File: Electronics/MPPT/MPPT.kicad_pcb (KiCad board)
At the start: 2 copper layers, 169.5 x 123.8 mm, 128 parts, among them J1 Solar Array, J2 Battery, J3 Car Power, J4 CAN_In, J5 CAN_Out, Q1 200N25N, Q2 200N25N, SW1 RESET, SW2 CAN Address, U1 PQMC3-D12-S9-S, U2 Nucleo_L432KC, U3 UCC37321, U4 INA210, U5 ADM3055E, U6 INA210, U7 CDSOT23-T24CAN

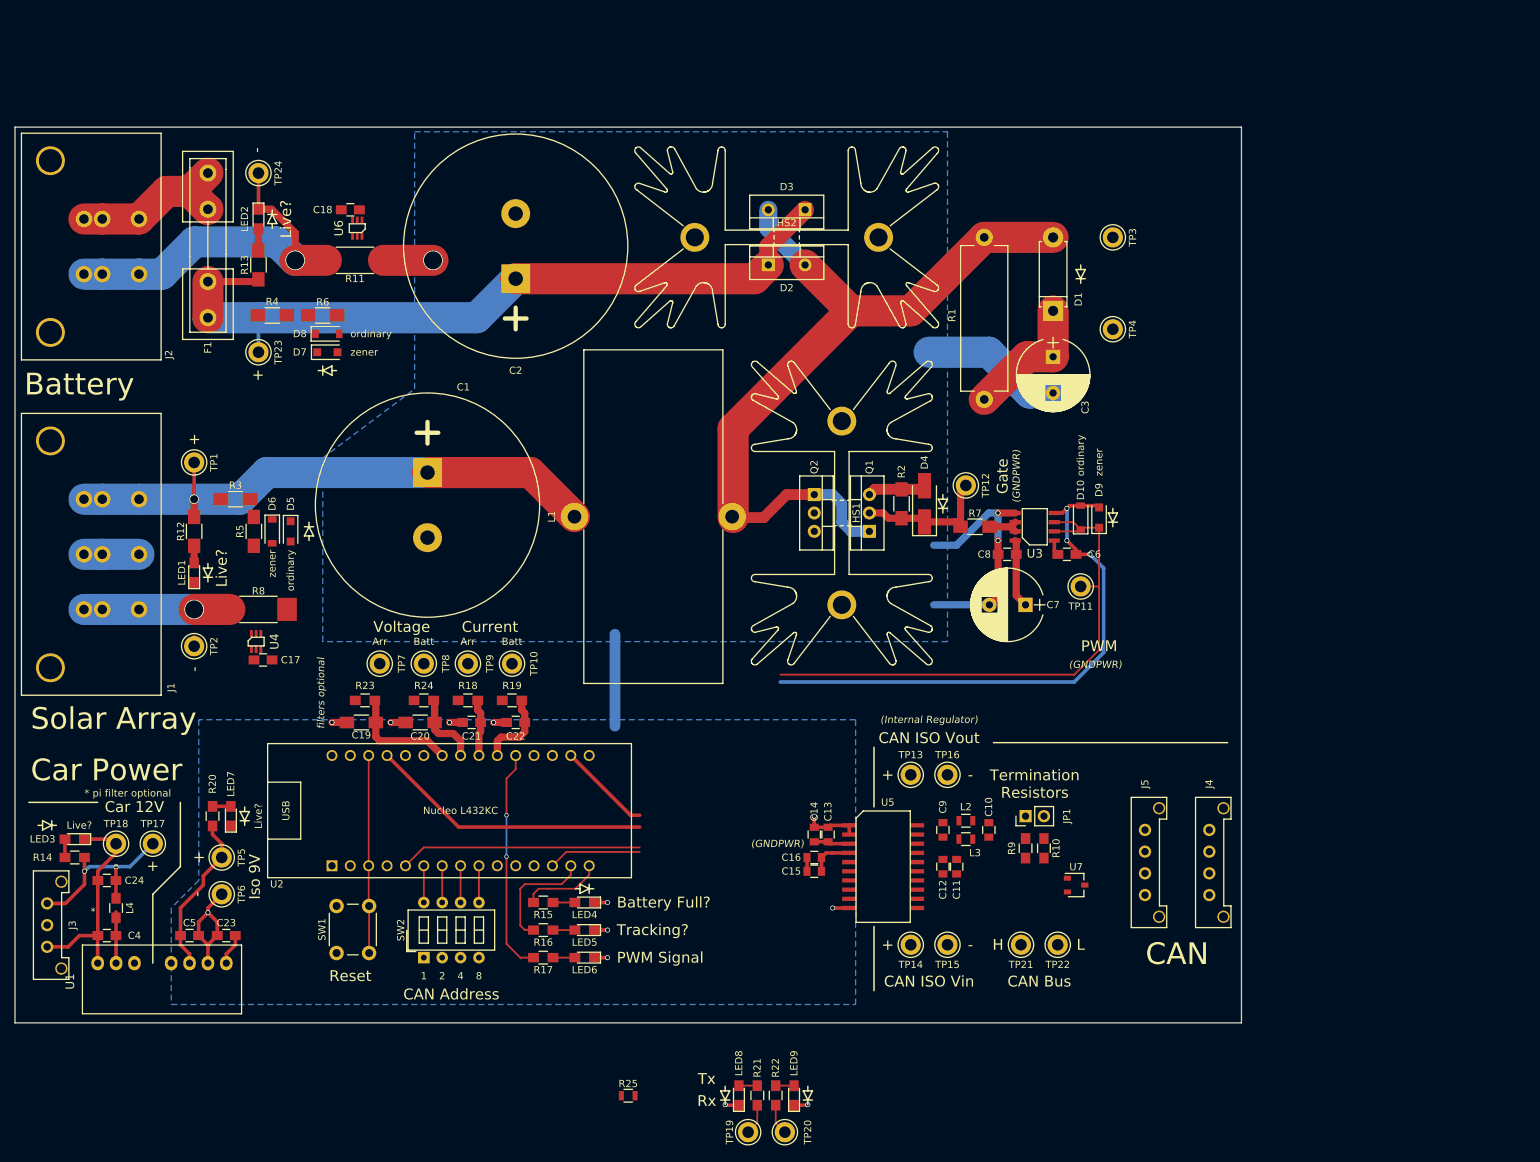
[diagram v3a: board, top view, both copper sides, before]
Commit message: MPPT: Moved CAN block to more compact location; shrunk board size.
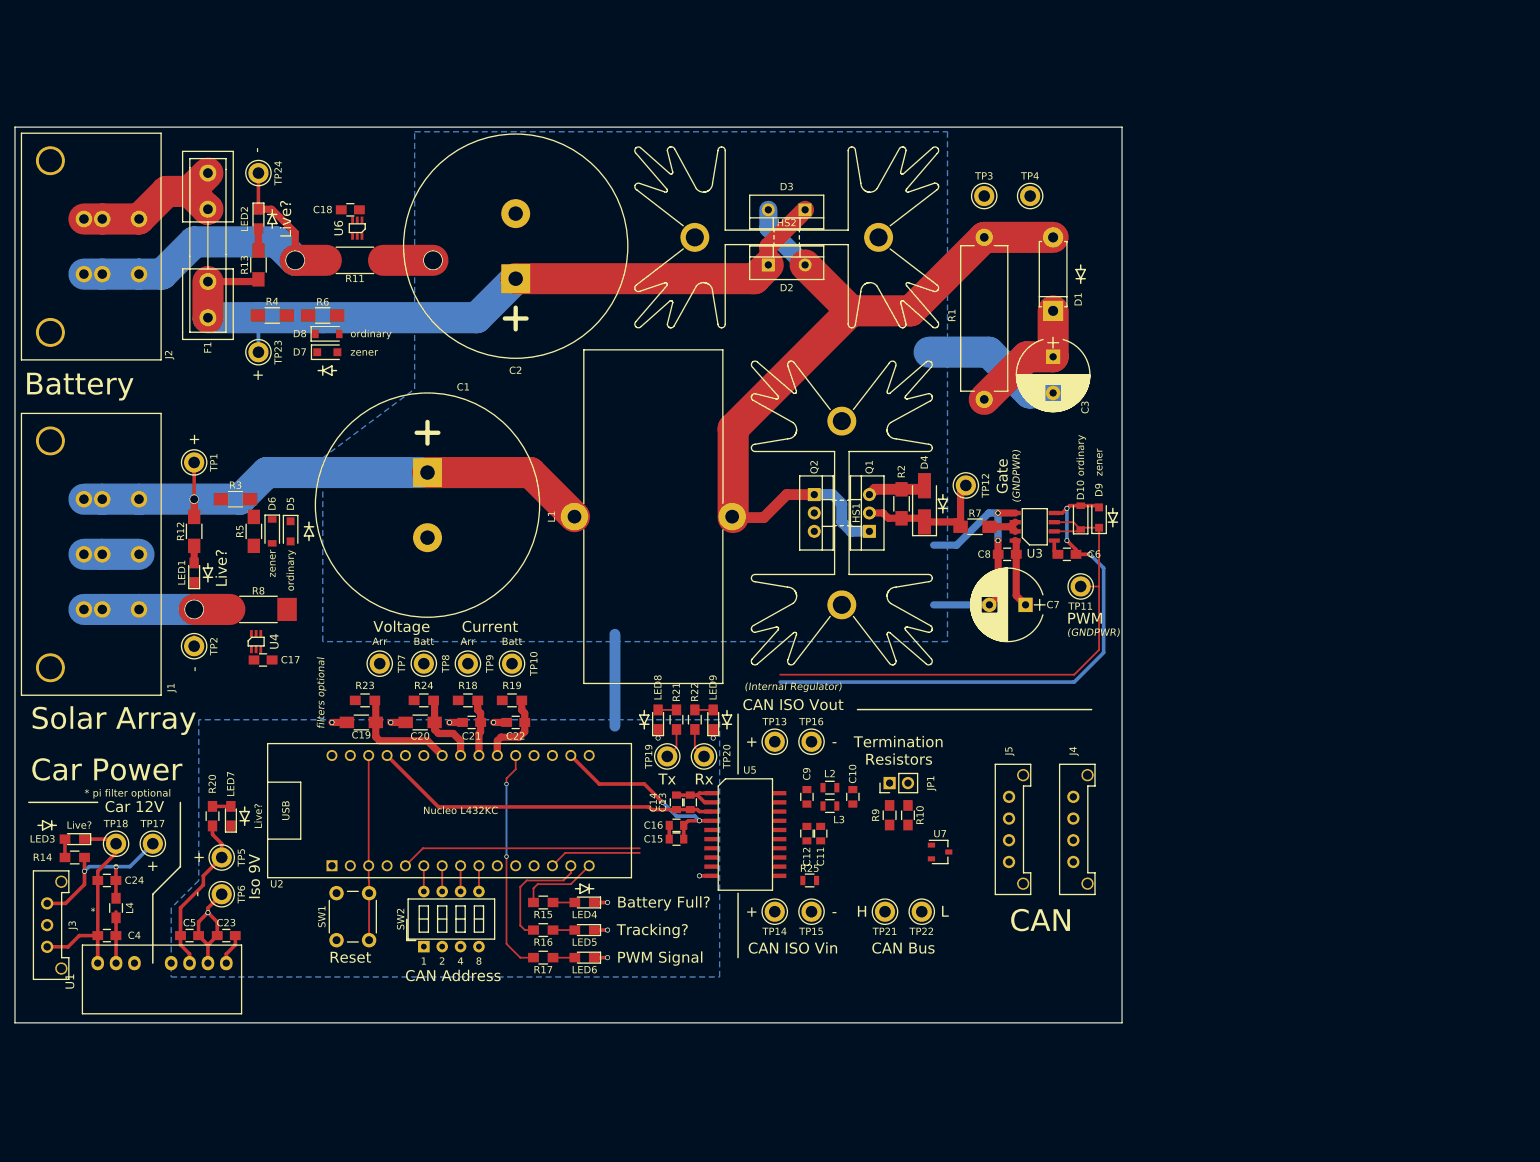
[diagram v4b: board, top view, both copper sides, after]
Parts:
- moved LED8 53.1 mm to (120.0, 113.0)
- moved LED9 53.1 mm to (127.6, 113.0)
- moved R21 53.1 mm to (122.6, 113.0)
- moved R22 53.1 mm to (125.1, 113.0)
- moved REF** 53.1 mm to (129.5, 113.0)
- moved REF** 53.1 mm to (118.1, 113.0)
- moved TP19 53.1 mm to (121.3, 118.1)
- moved TP20 53.1 mm to (126.4, 118.1)
- moved R25 38.9 mm to (141.0, 135.3)
- moved TP4 21.7 mm to (171.4, 40.6), turned to 0 degrees
- moved C13 19.6 mm to (124.5, 124.5)
- moved C15 19.6 mm to (122.6, 129.5)
- moved C14 19.6 mm to (122.6, 124.5)
- moved C16 19.6 mm to (122.6, 127.6)
- moved U5 19.6 mm to (132.1, 128.9)
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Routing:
- net +3V3: track 18.9 -> 27.5 mm, vias 0 -> 2
- net +5V: track 44.0 -> 48.0 mm
- net GNDPWR: track 189.9 -> 187.4 mm, vias 18 -> 17
- net /Reset: track 27.3 -> 25.5 mm
- net Net-(SW2-Pad8): track 5.08 -> 3.56 mm
- net Net-(SW2-Pad7): track 5.08 -> 3.56 mm
- net Net-(SW2-Pad6): track 5.08 -> 3.56 mm
- net Net-(SW2-Pad5): track 5.08 -> 3.56 mm
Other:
- board size 169.5 x 123.8 mm -> 153 x 123.8 mm

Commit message: MPPT: Move Car Power and Solar Array blocks to more compact locations; resize board.
Board is now 4.7x6.0in, and that's likely final.
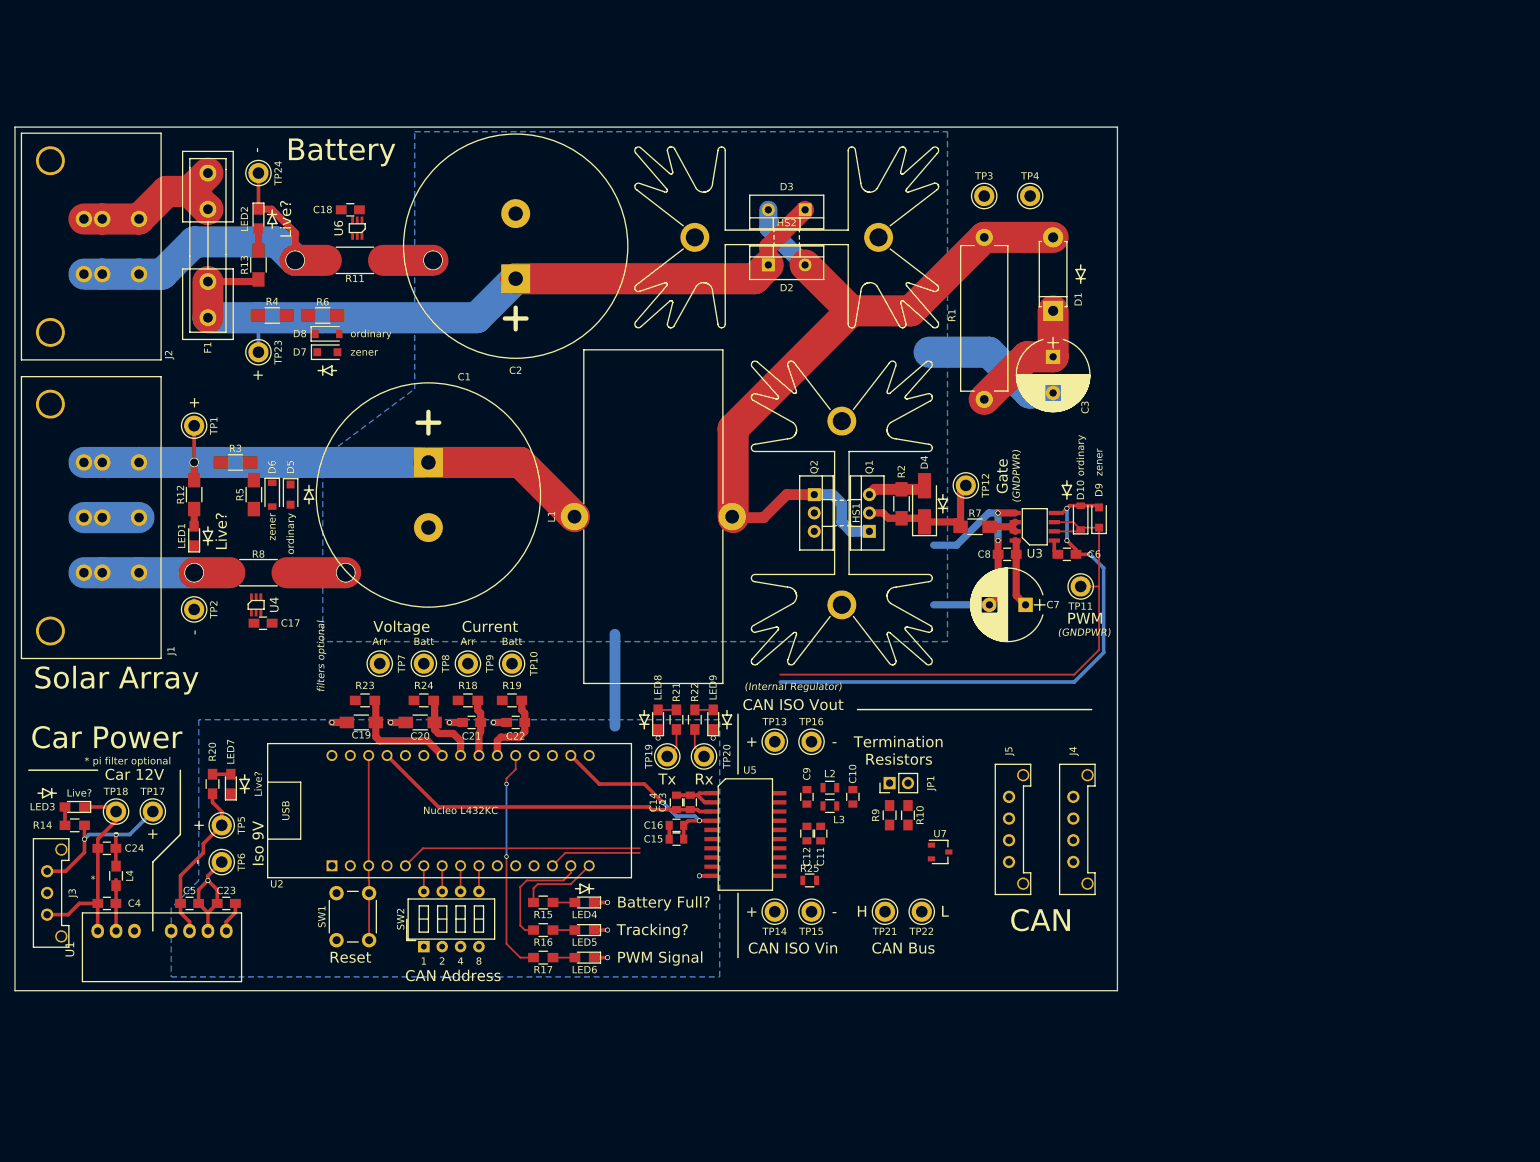
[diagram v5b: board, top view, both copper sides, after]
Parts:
- moved REF** 7.41 mm to (176.5, 81.3)
- moved C17 5.08 mm to (65.4, 99.7)
- moved R8 5.08 mm to (64.8, 92.7)
- moved D5 5.08 mm to (69.2, 81.9)
- moved D6 5.08 mm to (66.7, 81.9)
- moved J1 5.08 mm to (48.3, 77.5)
- moved LED1 5.08 mm to (55.9, 87.6)
- moved R12 5.08 mm to (55.9, 81.9)
- moved R3 5.08 mm to (61.6, 77.5)
- moved R5 5.08 mm to (64.1, 81.9)
- moved REF** 5.08 mm to (71.8, 81.9)
- moved REF** 5.08 mm to (57.8, 87.6)
- moved TP1 5.08 mm to (55.9, 72.4)
- moved TP2 5.08 mm to (55.9, 97.8)
- moved U4 5.08 mm to (64.4, 97.2)
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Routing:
- net GNDPWR: track 187.4 -> 195.5 mm, vias 17 -> 18
- net /+Arr: track 79.4 -> 78.4 mm
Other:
- board size 153 x 123.8 mm -> 152.4 x 119.4 mm

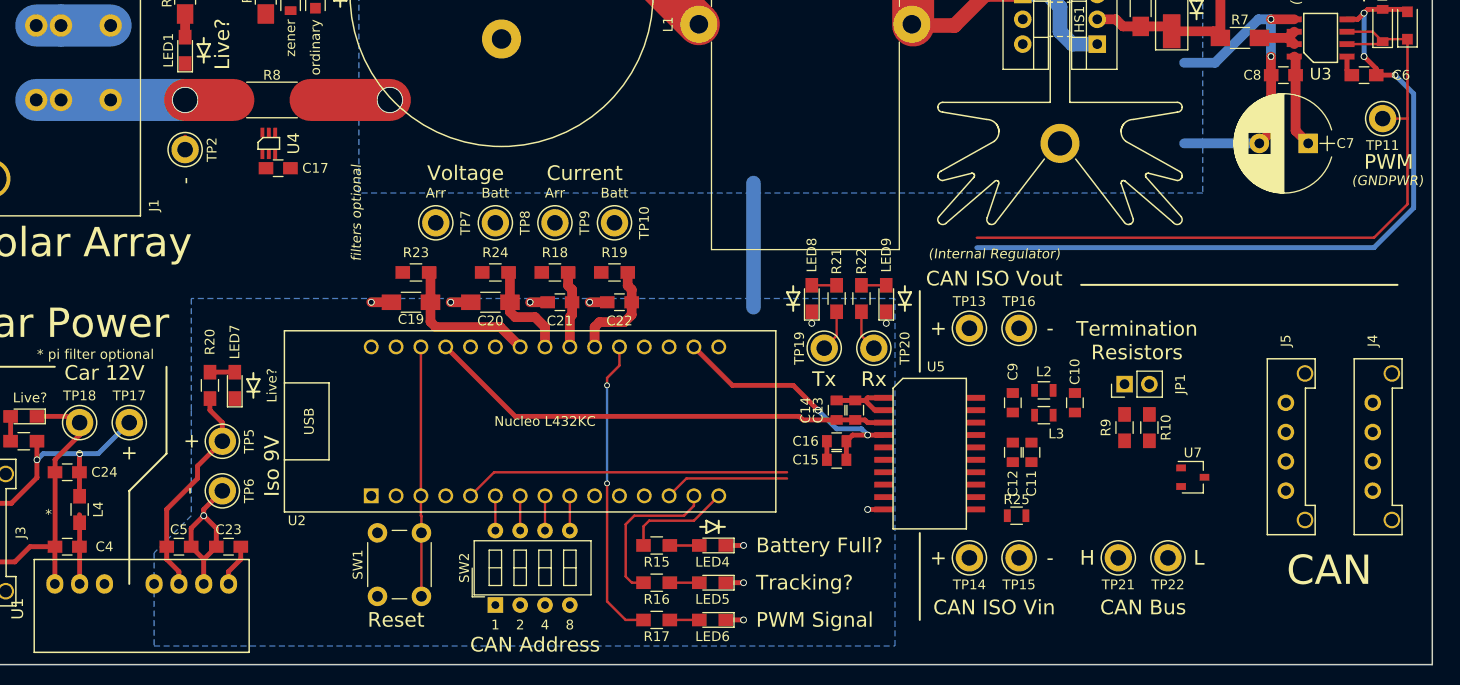
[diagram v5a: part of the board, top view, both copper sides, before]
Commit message: MPPT: Wire up CAN block; Change some CAN footprints to handsoldering variants.
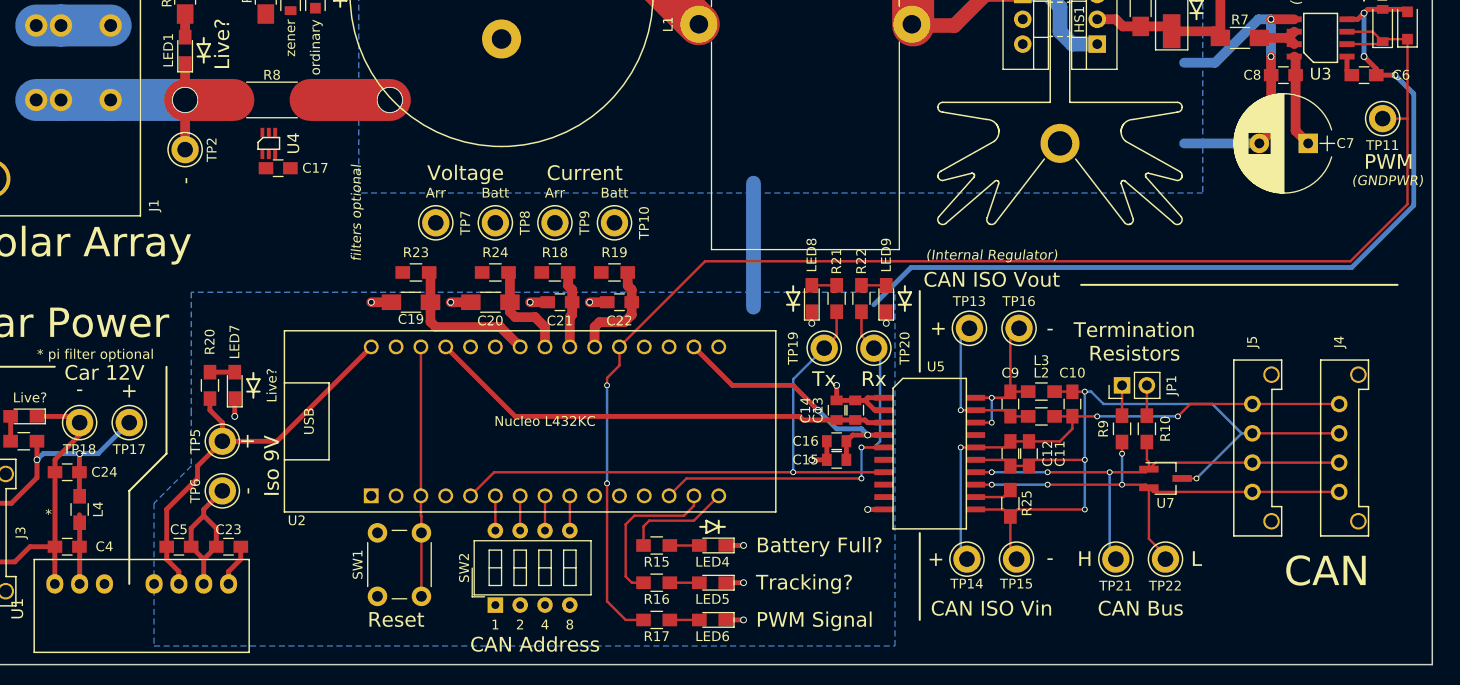
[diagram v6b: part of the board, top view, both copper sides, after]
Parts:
- C10, C11, C12, C9: footprint Capacitors_SMD:C_0805 -> Capacitors_SMD:C_0805_HandSoldering
- L2, L3: footprint Inductors_SMD:L_0805 -> Inductors_SMD:L_0805_HandSoldering
- R25: footprint Resistors_SMD:R_0805 -> Resistors_SMD:R_0805_HandSoldering
- U7: footprint TO_SOT_Packages_SMD:SOT-23W -> TO_SOT_Packages_SMD:SOT-23W_Handsoldering
- moved J4 3.43 mm to (174.0, 123.8)
- moved J5 3.43 mm to (165.1, 123.8)
- moved U7 2.80 mm to (156.2, 131.4)
- moved L2 2.68 mm to (143.5, 125.1)
- moved L3 2.43 mm to (143.5, 122.6)
- moved R25 1.42 mm to (140.3, 134.0), turned to 270 degrees
- moved JP1 0.28 mm to (151.8, 121.9)
- moved R9 0.28 mm to (151.8, 126.4)
- moved TP14 0.28 mm to (135.9, 139.7)
- moved C10 0.28 mm to (146.7, 123.8), turned to 90 degrees
- moved C11 0.28 mm to (142.2, 128.9)
- moved C12 0.28 mm to (140.3, 128.9)
- moved C9 0.28 mm to (140.3, 123.8)
- moved R10 0.28 mm to (154.3, 126.4)
- moved TP15 0.28 mm to (141.0, 139.7)
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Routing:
- net Net-(C10-Pad2): track 0.00 -> 79.1 mm, vias 0 -> 4
- net Net-(C10-Pad1): track 0.00 -> 54.9 mm, vias 0 -> 3
- net Net-(J4-Pad4): track 0.00 -> 49.9 mm, vias 0 -> 4
- net Net-(J4-Pad3): track 0.00 -> 49.6 mm, vias 0 -> 3
- net /PWM: track 106.5 -> 147.7 mm
- net /CAN_Rx: track 17.1 -> 42.1 mm, vias 0 -> 2
- net /CAN_Tx: track 37.6 -> 61.6 mm, vias 0 -> 1
- net +9VA: track 34.0 -> 53.2 mm
- net GNDPWR: track 195.5 -> 213.3 mm, vias 18 -> 20
- net Net-(C9-Pad2): track 0.00 -> 16.7 mm, vias 0 -> 2
- net Net-(C9-Pad1): track 0.00 -> 15.9 mm, vias 0 -> 1
- net /-Arr: track 21.5 -> 30.3 mm
- net Net-(R25-Pad1): track 0.00 -> 3.85 mm
- net Net-(JP1-Pad2): track 0.00 -> 3.09 mm
- net Net-(JP1-Pad1): track 0.00 -> 3.09 mm
